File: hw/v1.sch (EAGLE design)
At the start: 43 parts, among them J1 FFC2B28-24-G, J2 S2B-PH-SM4-TB(LF)(SN), J3 10118193-0001LF, J4 PTS636_SM25F_SMTR_LFS, Q1 SI1308EDL-T1-GE3, U1 ESP32-C3-WROOM-02-H4, U2 PCF85063ATT/AJ, U3 TLV1117LV33DCYR

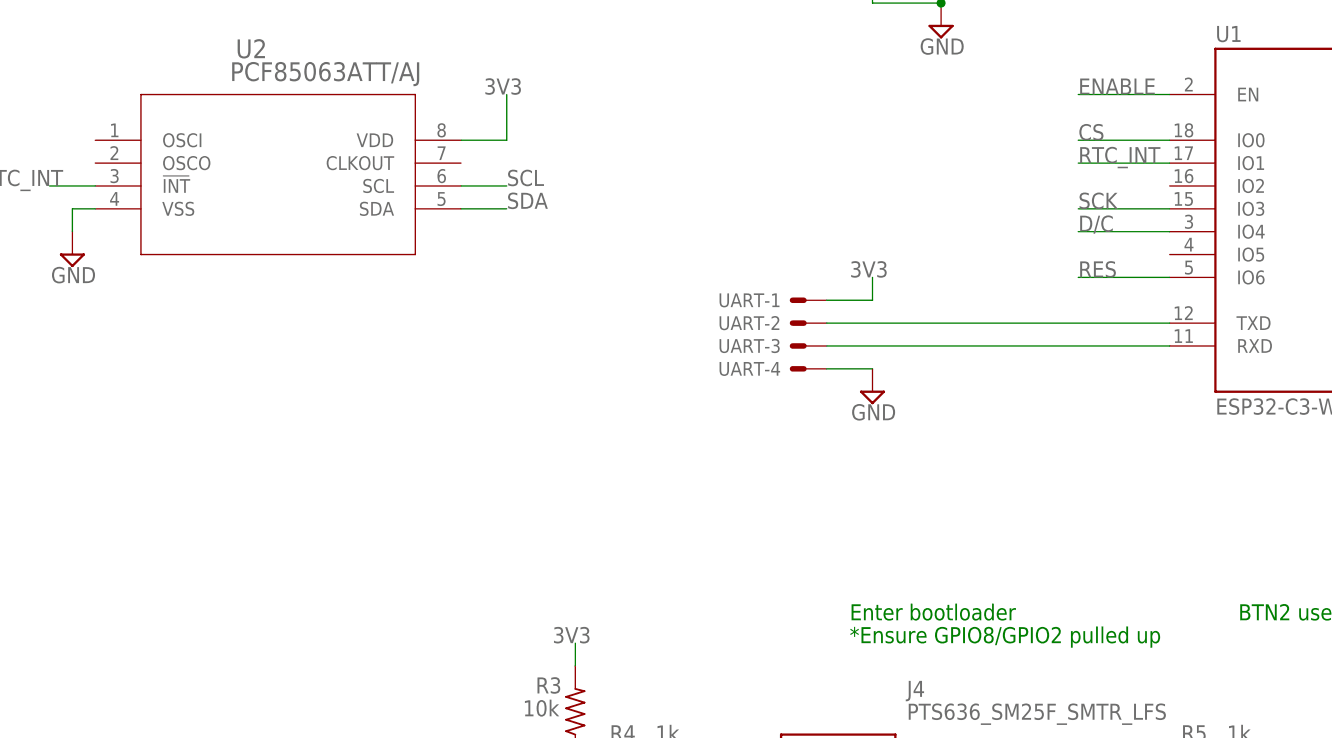
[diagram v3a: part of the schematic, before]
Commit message: Add temperature sensor
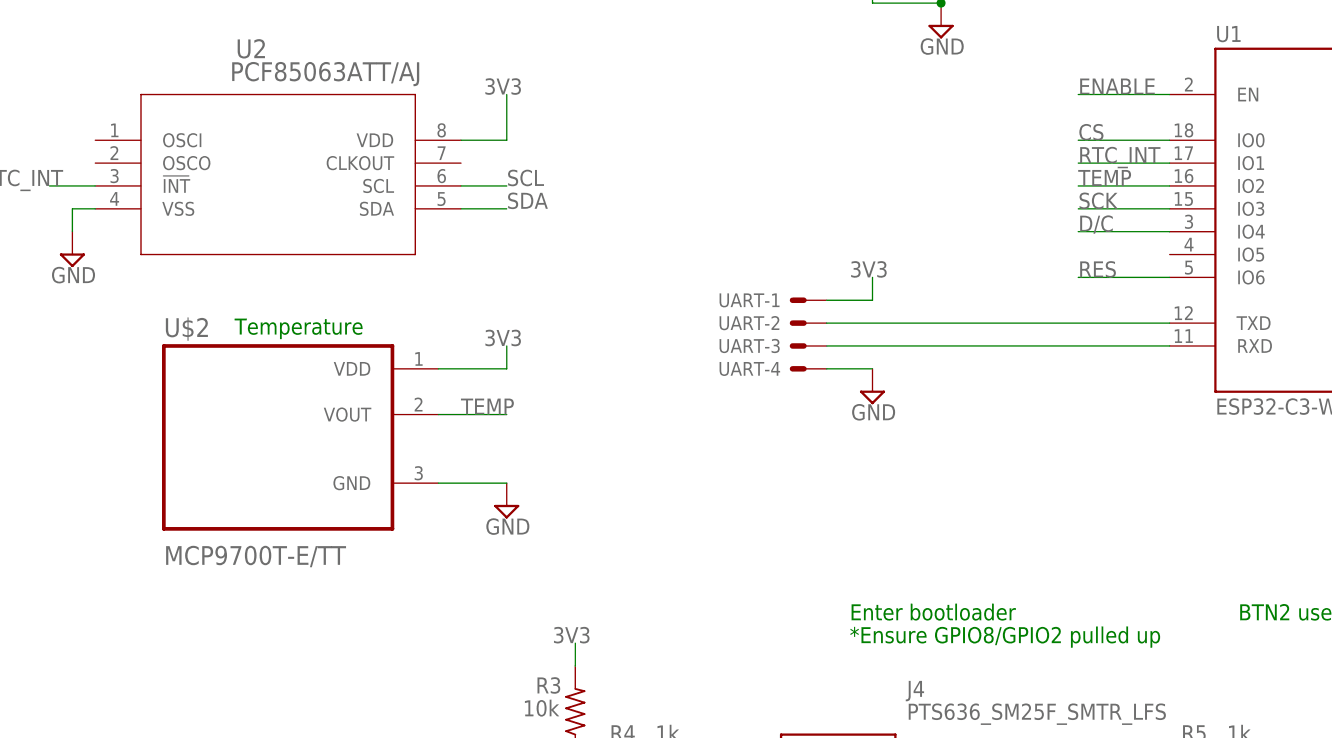
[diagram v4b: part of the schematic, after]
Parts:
- added U$2: MCP9700T-E/TT, MCP9700T-E_TT:MCP9700T-E/TT
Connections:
- new net TEMP: U$2.VOUT, U1.IO2
- net 3V3: now also U$2.VDD
- net GND: now also U$2.GND
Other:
- note added: "Temperature"
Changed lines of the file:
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@@
 <part name="S2" library="EVQ-P7A01P" deviceset="EVQ-P7A01P" device=""/>
 <part name="J4" library="PTS636_SM25F_SMTR_LFS" deviceset="PTS636_SM25F_SMTR_LFS" device=""/>
+<part name="U$2" library="MCP9700T-E_TT" deviceset="MCP9700T-E/TT" device=""/>
+<part name="SUPPLY22" library="Tutorial - Fusion 360" library_urn="urn:adsk.eagle:library:16997205" deviceset="GND" device="" value="GND"/>
 </parts>
 <sheets>
@@
 <text x="17.78" y="111.76" size="1.778" layer="91">E-ink Display</text>
 <text x="-10.16" y="-43.18" size="1.778" layer="91">BTN2 used for boot</text>
+<text x="-121.666" y="-11.43" size="1.778" layer="91">Temperature</text>
 </plain>
 <instances>
@@
 <attribute name="NAME" x="-46.99" y="-50.8" size="1.778" layer="95" align="center-left"/>
 <attribute name="VALUE" x="-46.99" y="-53.34" size="1.778" layer="96" align="center-left"/>
+</instance>
+<instance part="U$2" gate="A" x="-116.84" y="-22.86" smashed="yes">
+<attribute name="NAME" x="-129.54" y="-11.7" size="2.0828" layer="95" ratio="10" rot="SR0"/>
+<attribute name="VALUE" x="-129.54" y="-37.02" size="2.0828" layer="96" ratio="10" rot="SR0"/>
+</instance>
+<instance part="SUPPLY22" gate="G$1" x="-91.44" y="-30.48" smashed="yes">
+<attribute name="VALUE" x="-91.313" y="-33.655" size="1.778" layer="96" align="bottom-center"/>
 </instance>
 </instances>
@@
 <junction x="149.86" y="7.62"/>
 <label x="147.32" y="10.16" size="1.778" layer="95"/>
+</segment>
+<segment>
+<pinref part="U$2" gate="A" pin="VDD"/>
+<wire x1="-99.06" y1="-15.24" x2="-91.44" y2="-15.24" width="0.1524" layer="91"/>
+<wire x1="-91.44" y1="-15.24" x2="-91.44" y2="-12.7" width="0.1524" layer="91"/>
+<label x="-93.98" y="-12.7" size="1.778" layer="95"/>
 </segment>
 </net>
@@
 <wire x1="17.78" y1="-83.82" x2="12.7" y2="-83.82" width="0.1524" layer="91"/>
 </segment>
+<segment>
+<pinref part="U$2" gate="A" pin="GND"/>
+<wire x1="-99.06" y1="-27.94" x2="-91.44" y2="-27.94" width="0.1524" layer="91"/>
+<pinref part="SUPPLY22" gate="G$1" pin="GND"/>
+</segment>
 </net>
 <net name="N$7" class="0">
@@
 </segment>
 </net>
+<net name="TEMP" class="0">
+<segment>
+<pinref part="U$2" gate="A" pin="VOUT"/>
+<wire x1="-99.06" y1="-20.32" x2="-91.44" y2="-20.32" width="0.1524" layer="91"/>
+<label x="-96.52" y="-20.32" size="1.778" layer="95"/>
+</segment>
+<segment>
+<pinref part="U1" gate="G$1" pin="IO2"/>
+<wire x1="-17.78" y1="5.08" x2="-27.94" y2="5.08" width="0.1524" layer="91"/>
+<label x="-27.94" y="5.08" size="1.778" layer="95"/>
+</segment>
+</net>

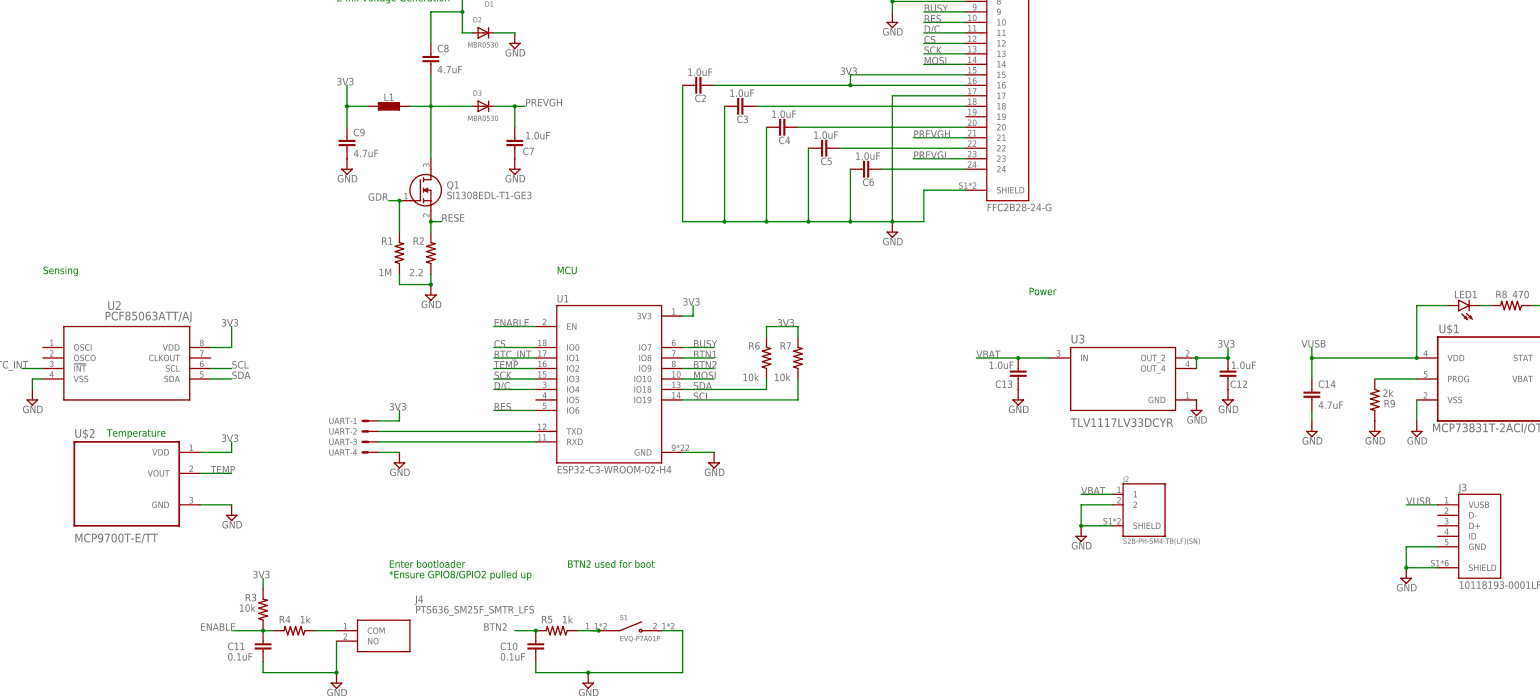
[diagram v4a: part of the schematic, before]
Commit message: Change inductor, add part numbers to bom
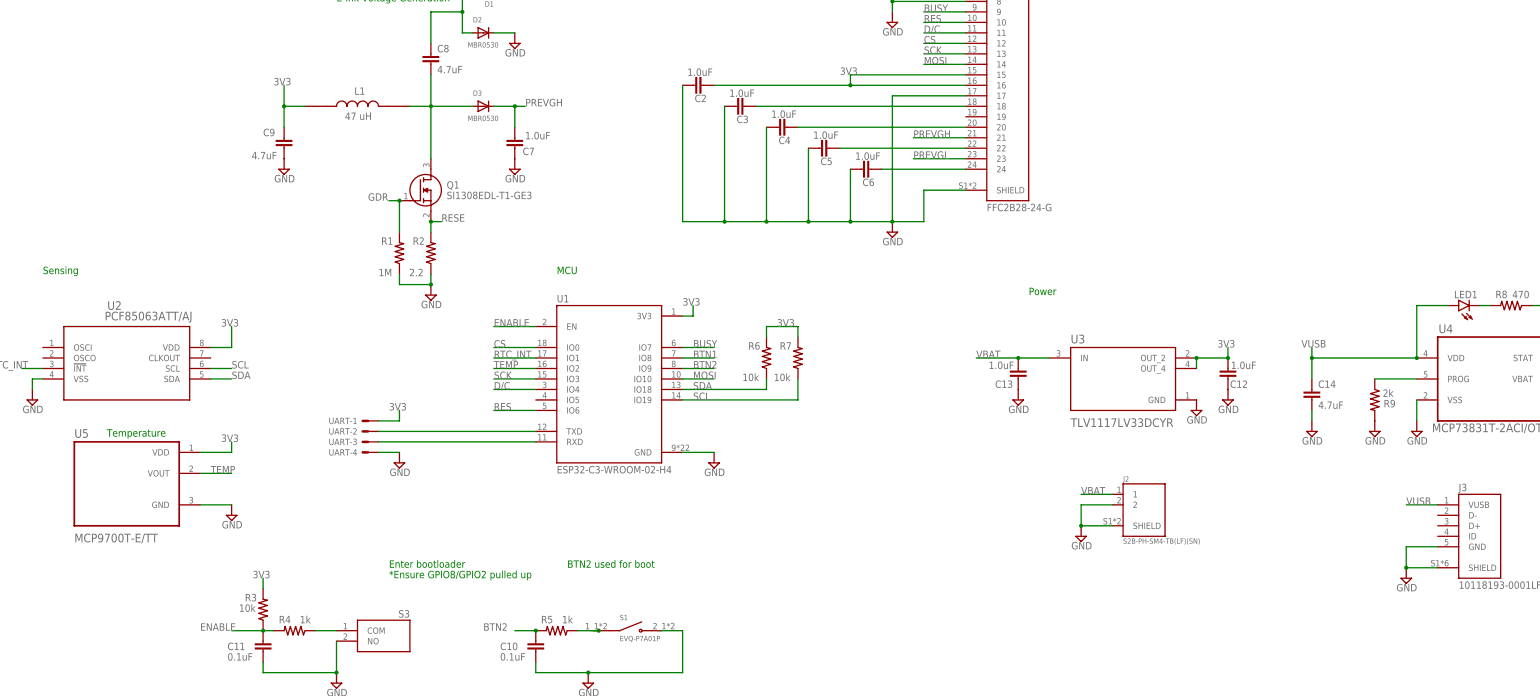
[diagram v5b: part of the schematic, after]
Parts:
- L1: value (none) -> 47 uH; device we-power:INDUCTOR-NR40XX -> ADL3225V-470MT-TL000:ADL3225V-470MT-TL000
- renumbered J4 to S3, U$1 to U4, U$2 to U5
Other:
- moved on the sheet: C9
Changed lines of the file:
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@@
 <part name="C7" library="SparkFun-Capacitors" deviceset="1.0UF" device="-0603-16V-10%-X7R-WE" value="1.0uF"/>
 <part name="SUPPLY4" library="Tutorial - Fusion 360" library_urn="urn:adsk.eagle:library:16997205" deviceset="GND" device="" value="GND"/>
-<part name="L1" library="we-power" deviceset="INDUCTOR" device="-NR40XX"/>
 <part name="C9" library="SparkFun-Capacitors" deviceset="4.7UF" device="-0603-35V-(20%)" value="4.7uF"/>
 <part name="SUPPLY5" library="Tutorial - Fusion 360" library_urn="urn:adsk.eagle:library:16997205" deviceset="GND" device="" value="GND"/>
@@
 <part name="J2" library="S2B-PH-SM4-TB_LF__SN_" deviceset="S2B-PH-SM4-TB(LF)(SN)" device=""/>
 <part name="SUPPLY15" library="Tutorial - Fusion 360" library_urn="urn:adsk.eagle:library:16997205" deviceset="GND" device="" value="GND"/>
-<part name="U$1" library="MCP73831T-2ACI_OT" deviceset="MCP73831T-2ACI/OT" device=""/>
+<part name="U4" library="MCP73831T-2ACI_OT" deviceset="MCP73831T-2ACI/OT" device=""/>
 <part name="C14" library="SparkFun-Capacitors" deviceset="4.7UF" device="-0603-35V-(20%)" value="4.7uF"/>
 <part name="LED1" library="led" library_urn="urn:adsk.eagle:library:259" deviceset="LED" device="CHIP-LED0603" package3d_urn="urn:adsk.eagle:package:15819/3"/>
@@
 <part name="S1" library="EVQ-P7A01P" deviceset="EVQ-P7A01P" device=""/>
 <part name="S2" library="EVQ-P7A01P" deviceset="EVQ-P7A01P" device=""/>
-<part name="J4" library="PTS636_SM25F_SMTR_LFS" deviceset="PTS636_SM25F_SMTR_LFS" device=""/>
-<part name="U$2" library="MCP9700T-E_TT" deviceset="MCP9700T-E/TT" device=""/>
+<part name="S3" library="PTS636_SM25F_SMTR_LFS" deviceset="PTS636_SM25F_SMTR_LFS" device=""/>
+<part name="U5" library="MCP9700T-E_TT" deviceset="MCP9700T-E/TT" device=""/>
 <part name="SUPPLY22" library="Tutorial - Fusion 360" library_urn="urn:adsk.eagle:library:16997205" deviceset="GND" device="" value="GND"/>
+<part name="L1" library="ADL3225V-470MT-TL000" deviceset="ADL3225V-470MT-TL000" device="" value="47 uH"/>
 </parts>
 <sheets>
@@
 <attribute name="VALUE" x="-22.733" y="50.165" size="1.778" layer="96" align="bottom-center"/>
 </instance>
-<instance part="L1" gate="L" x="-53.34" y="68.58" smashed="yes">
-<attribute name="NAME" x="-53.34" y="69.85" size="1.778" layer="95" align="bottom-center"/>
-<attribute name="VALUE" x="-53.34" y="67.31" size="1.778" layer="96" align="top-center"/>
-</instance>
-<instance part="C9" gate="G$1" x="-63.5" y="58.42" smashed="yes">
-<attribute name="NAME" x="-61.976" y="61.341" size="1.778" layer="95" font="vector"/>
-<attribute name="VALUE" x="-61.976" y="56.261" size="1.778" layer="96" font="vector"/>
-</instance>
-<instance part="SUPPLY5" gate="G$1" x="-63.5" y="53.34" smashed="yes">
-<attribute name="VALUE" x="-63.373" y="50.165" size="1.778" layer="96" align="bottom-center"/>
+<instance part="C9" gate="G$1" x="-78.74" y="58.42" smashed="yes">
+<attribute name="NAME" x="-83.82" y="61.341" size="1.778" layer="95" font="vector"/>
+<attribute name="VALUE" x="-86.614" y="55.753" size="1.778" layer="96" font="vector"/>
+</instance>
+<instance part="SUPPLY5" gate="G$1" x="-78.74" y="53.34" smashed="yes">
+<attribute name="VALUE" x="-78.613" y="50.165" size="1.778" layer="96" align="bottom-center"/>
 </instance>
 <instance part="Q1" gate="G$1" x="-50.8" y="45.72" smashed="yes">
@@
 <attribute name="VALUE" x="114.427" y="-38.735" size="1.778" layer="96" align="bottom-center"/>
 </instance>
-<instance part="U$1" gate="A" x="213.36" y="5.08" smashed="yes">
+<instance part="U4" gate="A" x="213.36" y="5.08" smashed="yes">
 <attribute name="NAME" x="200.855259375" y="13.6338" size="2.08681875" layer="95" ratio="10" rot="SR0"/>
 <attribute name="VALUE" x="199.27943125" y="-10.3383" size="2.085940625" layer="96" ratio="10" rot="SR0"/>
@@
 <attribute name="VALUE" x="2.54" y="-86.36" size="1.27" layer="96"/>
 </instance>
-<instance part="J4" gate="G$1" x="-66.04" y="-58.42" smashed="yes">
-<attribute name="NAME" x="-46.99" y="-50.8" size="1.778" layer="95" align="center-left"/>
-<attribute name="VALUE" x="-46.99" y="-53.34" size="1.778" layer="96" align="center-left"/>
-</instance>
-<instance part="U$2" gate="A" x="-116.84" y="-22.86" smashed="yes">
+<instance part="S3" gate="G$1" x="-66.04" y="-58.42" smashed="yes">
+<attribute name="NAME" x="-51.054" y="-54.356" size="1.778" layer="95" align="center-left"/>
+</instance>
+<instance part="U5" gate="A" x="-116.84" y="-22.86" smashed="yes">
 <attribute name="NAME" x="-129.54" y="-11.7" size="2.0828" layer="95" ratio="10" rot="SR0"/>
 <attribute name="VALUE" x="-129.54" y="-37.02" size="2.0828" layer="96" ratio="10" rot="SR0"/>
@@
 <instance part="SUPPLY22" gate="G$1" x="-91.44" y="-30.48" smashed="yes">
 <attribute name="VALUE" x="-91.313" y="-33.655" size="1.778" layer="96" align="bottom-center"/>
+</instance>
+<instance part="L1" gate="G$1" x="-60.96" y="68.58" smashed="yes">
+<attribute name="NAME" x="-61.722" y="71.374" size="1.778" layer="95"/>
+<attribute name="VALUE" x="-64.008" y="67.056" size="1.778" layer="96" align="top-left"/>
 </instance>
 </instances>
@@
 </segment>
 <segment>
-<pinref part="L1" gate="L" pin="1"/>
-<wire x1="-58.42" y1="68.58" x2="-63.5" y2="68.58" width="0.1524" layer="91"/>
-<wire x1="-63.5" y1="68.58" x2="-63.5" y2="73.66" width="0.1524" layer="91"/>
+<wire x1="-73.66" y1="68.58" x2="-78.74" y2="68.58" width="0.1524" layer="91"/>
+<wire x1="-78.74" y1="68.58" x2="-78.74" y2="73.66" width="0.1524" layer="91"/>
 <pinref part="C9" gate="G$1" pin="1"/>
-<wire x1="-63.5" y1="63.5" x2="-63.5" y2="68.58" width="0.1524" layer="91"/>
-<junction x="-63.5" y="68.58"/>
-<label x="-66.04" y="73.66" size="1.778" layer="95"/>
+<wire x1="-78.74" y1="63.5" x2="-78.74" y2="68.58" width="0.1524" layer="91"/>
+<junction x="-78.74" y="68.58"/>
+<label x="-81.28" y="73.66" size="1.778" layer="95"/>
+<pinref part="L1" gate="G$1" pin="1"/>
 </segment>
 <segment>
@@
 </segment>
 <segment>
-<pinref part="U$2" gate="A" pin="VDD"/>
+<pinref part="U5" gate="A" pin="VDD"/>
 <wire x1="-99.06" y1="-15.24" x2="-91.44" y2="-15.24" width="0.1524" layer="91"/>
 <wire x1="-91.44" y1="-15.24" x2="-91.44" y2="-12.7" width="0.1524" layer="91"/>
@@
 <pinref part="C11" gate="G$1" pin="2"/>
 <junction x="-66.04" y="-68.58"/>
-<pinref part="J4" gate="G$1" pin="NO"/>
+<pinref part="S3" gate="G$1" pin="NO"/>
 <wire x1="-66.04" y1="-60.96" x2="-66.04" y2="-68.58" width="0.1524" layer="91"/>
 </segment>
@@
 </segment>
 <segment>
-<pinref part="U$1" gate="A" pin="VSS"/>
+<pinref part="U4" gate="A" pin="VSS"/>
 <pinref part="SUPPLY17" gate="G$1" pin="GND"/>
 <wire x1="195.58" y1="-7.62" x2="195.58" y2="-2.54" width="0.1524" layer="91"/>
@@
 </segment>
 <segment>
-<pinref part="U$2" gate="A" pin="GND"/>
+<pinref part="U5" gate="A" pin="GND"/>
 <wire x1="-99.06" y1="-27.94" x2="-91.44" y2="-27.94" width="0.1524" layer="91"/>
 <pinref part="SUPPLY22" gate="G$1" pin="GND"/>
@@
 <pinref part="D3" gate="G$1" pin="A"/>
 <wire x1="-43.18" y1="68.58" x2="-33.02" y2="68.58" width="0.1524" layer="91"/>
-<pinref part="L1" gate="L" pin="2"/>
 <wire x1="-48.26" y1="68.58" x2="-43.18" y2="68.58" width="0.1524" layer="91"/>
 <junction x="-43.18" y="68.58"/>
 <pinref part="Q1" gate="G$1" pin="D"/>
 <wire x1="-43.18" y1="68.58" x2="-43.18" y2="55.88" width="0.1524" layer="91"/>
+<pinref part="L1" gate="G$1" pin="2"/>
 </segment>
 </net>
@@
 </segment>
 <segment>
-<pinref part="U$1" gate="A" pin="VBAT"/>
+<pinref part="U4" gate="A" pin="VBAT"/>
 <pinref part="C15" gate="G$1" pin="1"/>
 <wire x1="231.14" y1="2.54" x2="241.3" y2="2.54" width="0.1524" layer="91"/>
@@
 <net name="VUSB" class="0">
 <segment>
-<pinref part="U$1" gate="A" pin="VDD"/>
+<pinref part="U4" gate="A" pin="VDD"/>
 <wire x1="195.58" y1="7.62" x2="195.58" y2="20.32" width="0.1524" layer="91"/>
 <pinref part="LED1" gate="G$1" pin="A"/>
@@
 <wire x1="223.52" y1="20.32" x2="231.14" y2="20.32" width="0.1524" layer="91"/>
 <wire x1="231.14" y1="20.32" x2="231.14" y2="7.62" width="0.1524" layer="91"/>
-<pinref part="U$1" gate="A" pin="STAT"/>
+<pinref part="U4" gate="A" pin="STAT"/>
 </segment>
 </net>
 <net name="N$15" class="0">
 <segment>
-<pinref part="U$1" gate="A" pin="PROG"/>
+<pinref part="U4" gate="A" pin="PROG"/>
 <pinref part="R9" gate="G$1" pin="1"/>
 <wire x1="195.58" y1="2.54" x2="185.42" y2="2.54" width="0.1524" layer="91"/>
@@
 <segment>
 <pinref part="R4" gate="G$1" pin="1"/>
-<pinref part="J4" gate="G$1" pin="COM"/>
+<pinref part="S3" gate="G$1" pin="COM"/>
 <wire x1="-71.12" y1="-58.42" x2="-66.04" y2="-58.42" width="0.1524" layer="91"/>
 </segment>
@@
 <net name="TEMP" class="0">
 <segment>
-<pinref part="U$2" gate="A" pin="VOUT"/>
+<pinref part="U5" gate="A" pin="VOUT"/>
 <wire x1="-99.06" y1="-20.32" x2="-91.44" y2="-20.32" width="0.1524" layer="91"/>
 <label x="-96.52" y="-20.32" size="1.778" layer="95"/>

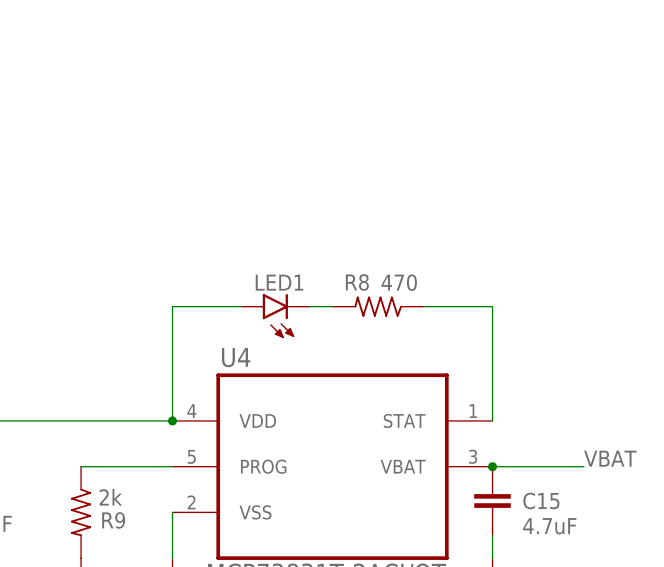
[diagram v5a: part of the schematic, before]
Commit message: Find passive parts, change led resistor to 300 ohm
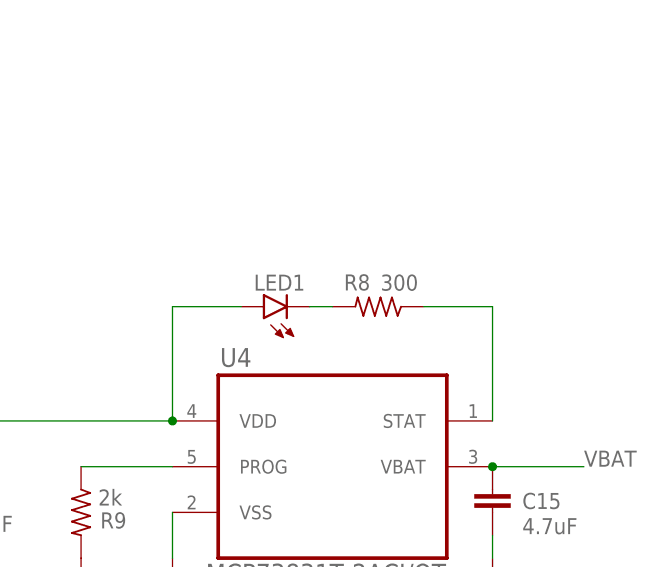
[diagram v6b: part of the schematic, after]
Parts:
- R8: value 470 -> 300
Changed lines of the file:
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@@
 <part name="C14" library="SparkFun-Capacitors" deviceset="4.7UF" device="-0603-35V-(20%)" value="4.7uF"/>
 <part name="LED1" library="led" library_urn="urn:adsk.eagle:library:259" deviceset="LED" device="CHIP-LED0603" package3d_urn="urn:adsk.eagle:package:15819/3"/>
-<part name="R8" library="rcl" library_urn="urn:adsk.eagle:library:334" deviceset="R-US_" device="R0603" package3d_urn="urn:adsk.eagle:package:23555/3" value="470"/>
+<part name="R8" library="rcl" library_urn="urn:adsk.eagle:library:334" deviceset="R-US_" device="R0603" package3d_urn="urn:adsk.eagle:package:23555/3" value="300"/>
 <part name="SUPPLY16" library="Tutorial - Fusion 360" library_urn="urn:adsk.eagle:library:16997205" deviceset="GND" device="" value="GND"/>
 <part name="SUPPLY17" library="Tutorial - Fusion 360" library_urn="urn:adsk.eagle:library:16997205" deviceset="GND" device="" value="GND"/>
